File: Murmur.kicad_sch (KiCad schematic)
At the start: 2 parts, among them U1 ESP32-S3-MINI-1

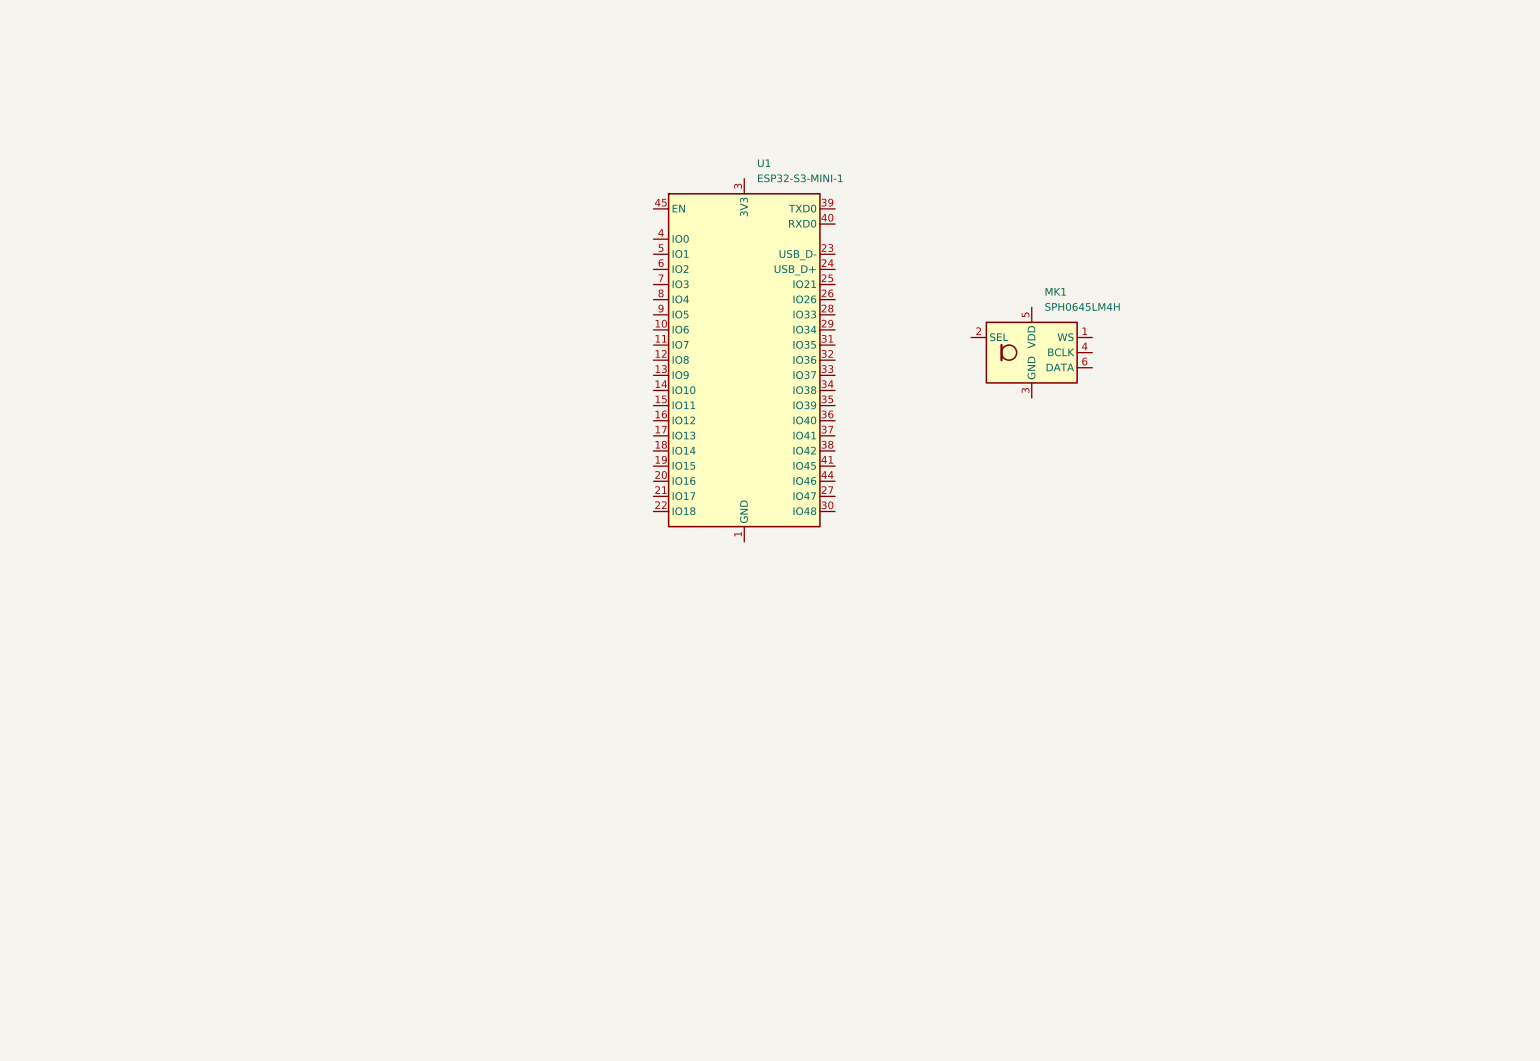
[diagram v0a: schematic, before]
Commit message: "Added new schematics, and started wiring the main components"
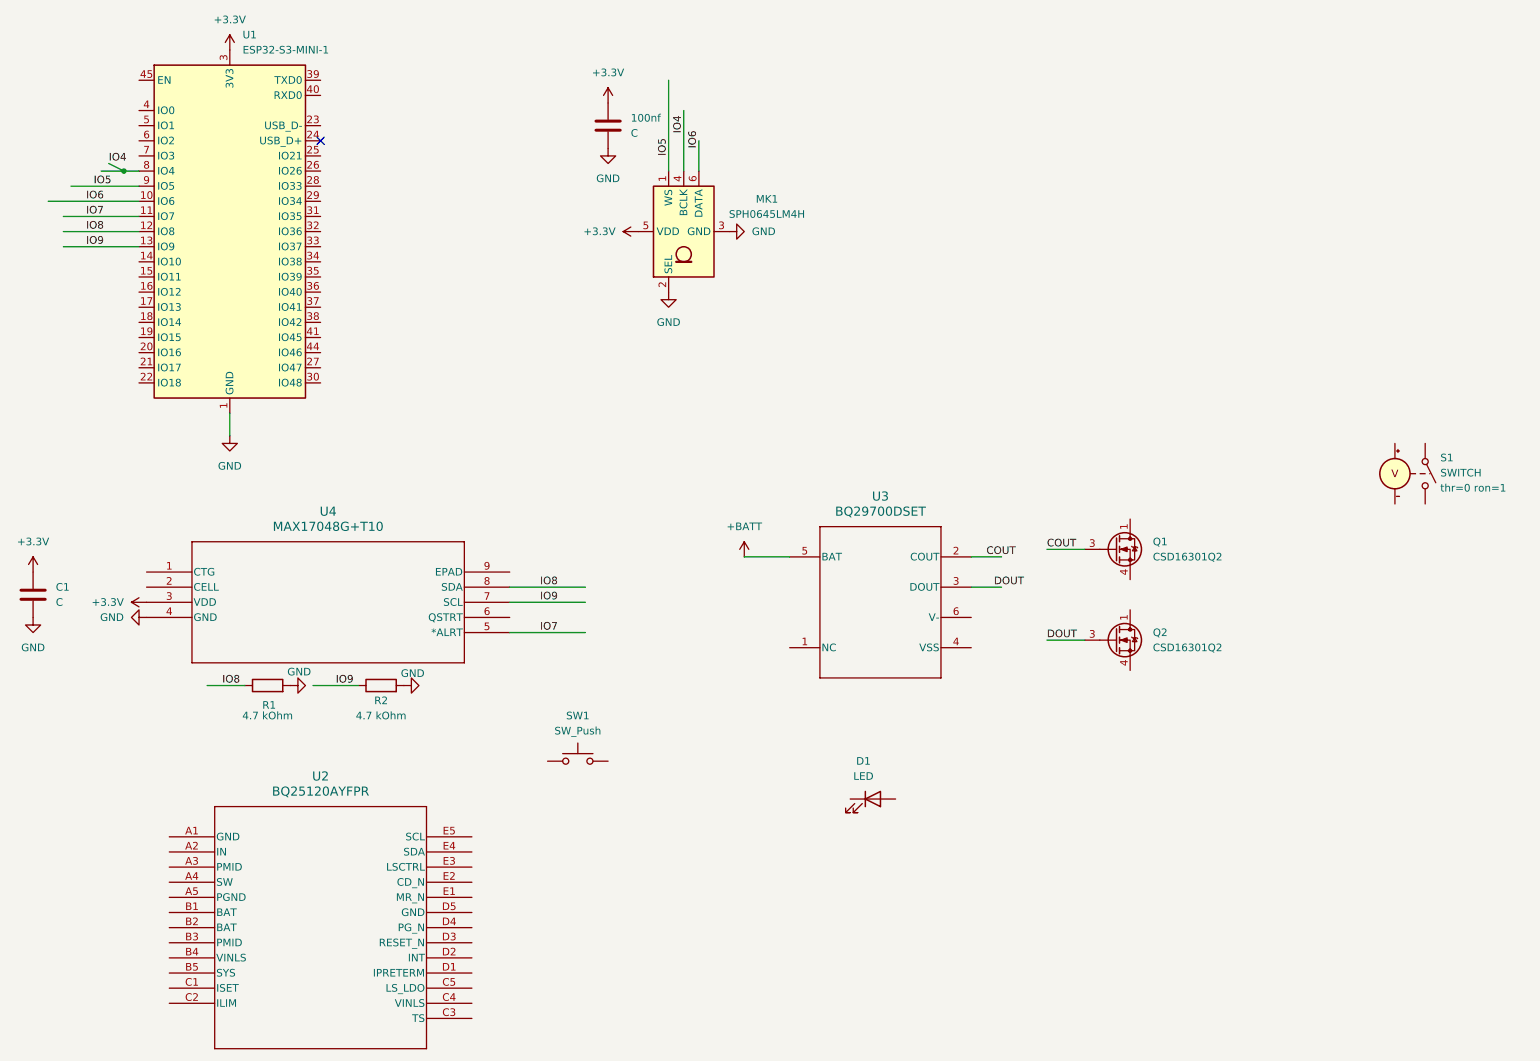
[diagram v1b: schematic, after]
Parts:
- added 100nf, C1: C, Package_TO_SOT_SMD:SOT-23-5, symbol Device:C
- added D1: LED, Package_SON:Texas_DQK, symbol Device:LED
- added Q1, Q2: CSD16301Q2, Package_SON:Texas_DQK, symbol Transistor_FET:CSD16301Q2
- added R1, R2: 4.7 kOhm, symbol Device:R
- added S1: SWITCH, Button_Switch_SMD:Nidec_Copal_CAS-120A, symbol Simulation_SPICE:SWITCH
- added SW1: SW_Push, symbol Switch:SW_Push
- added U2: BQ25120AYFPR, YFP0025BABD_TEX, symbol 2026-10-02_00-15-45:BQ25120AYFPR
- added U3: BQ29700DSET, DSE0006A, symbol 2026-10-02_00-59-19:BQ29700DSET
- added U4: MAX17048G+T10, 21-0168E_T822-3_MXM, symbol 2026-10-02_01-28-27:MAX17048G+T10
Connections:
- net GND: now reaches U1.1 (GND), U1.2 (GND), U1.42 (GND), U1.43 (GND), U1.46 (GND), U1.47 (GND), U1.48 (GND), U1.49 (GND), U1.50 (GND), U1.51 (GND), U1.52 (GND), U1.53 (GND), U1.54 (GND), U1.55 (GND), U1.56 (GND), U1.57 (GND), U1.58 (GND), U1.59 (GND), U1.60 (GND), U1.61 (GND), U1.62 (GND), U1.63 (GND), U1.64 (GND), U1.65 (GND)
- net GND: now also MK1.2 (SEL), MK1.3 (GND), 100nf.2, C1.2, R1.2, R2.2, U4.4 (GND)
- net IO6: now reaches U1.10 (IO6)
- net IO6: now also MK1.6 (DATA)
- net IO7: now reaches U1.11 (IO7)
- net IO7: now also U4.5 (*ALRT)
- net IO8: now reaches U1.12 (IO8)
- net IO8: now also R1.1, U4.8 (SDA)
- net IO9: now reaches U1.13 (IO9)
- net IO9: now also R2.1, U4.7 (SCL)
- net +3.3V: now reaches U1.3 (3V3)
- net +3.3V: now also MK1.5 (VDD), 100nf.1, C1.1, U4.3 (VDD)
- net IO4: now reaches U1.8 (IO4)
- net IO4: now also MK1.4 (BCLK)
- net IO5: now reaches U1.9 (IO5)
- net IO5: now also MK1.1 (WS)
- new net: Q1.1 (D), Q1.2 (D), Q1.5 (D), Q1.6 (D), Q1.8 (D)
- new net: Q1.4 (S), Q1.7 (S)
- new net: Q2.1 (D), Q2.2 (D), Q2.5 (D), Q2.6 (D), Q2.8 (D)
- new net: Q2.4 (S), Q2.7 (S)
- new net +BATT: U3.5 (BAT)
- new net COUT: Q1.3 (G), U3.2 (COUT)
- new net DOUT: Q2.3 (G), U3.3 (DOUT)
- no-connect marks 0 -> 1
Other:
- moved on the sheet: MK1, U1
